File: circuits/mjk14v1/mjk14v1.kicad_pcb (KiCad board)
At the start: 2 copper layers, 56.6 x 57.7 mm, 34 parts, among them J1 9VDC, J2 GND, J3 Touch, J4 Touch GND, Q1 MMBT100, Q2 MMBT100, Q3 MMBT100, Q4 MMBT100, U1 4093, U2 4029, U3 BAW56LT1G, U4 BAW56LT1G

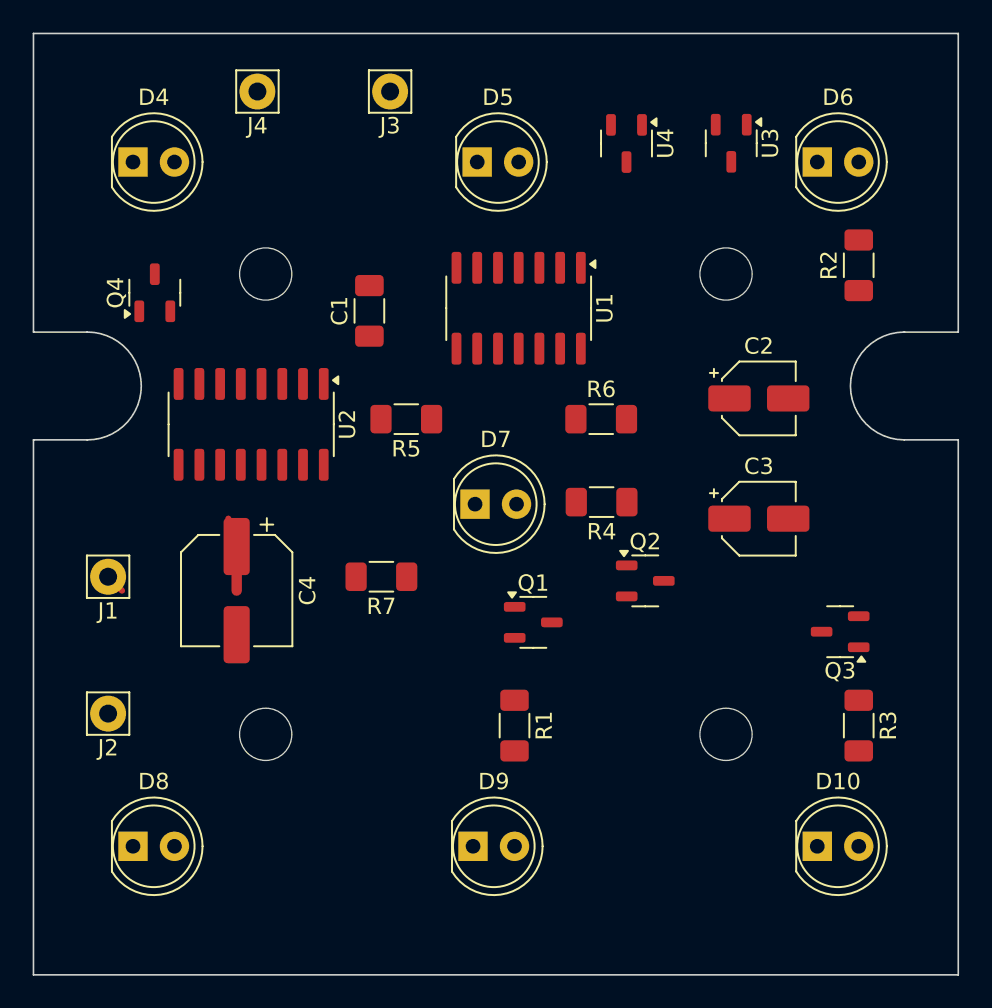
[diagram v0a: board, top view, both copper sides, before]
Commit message: Adding test points to the modernized JK14 design
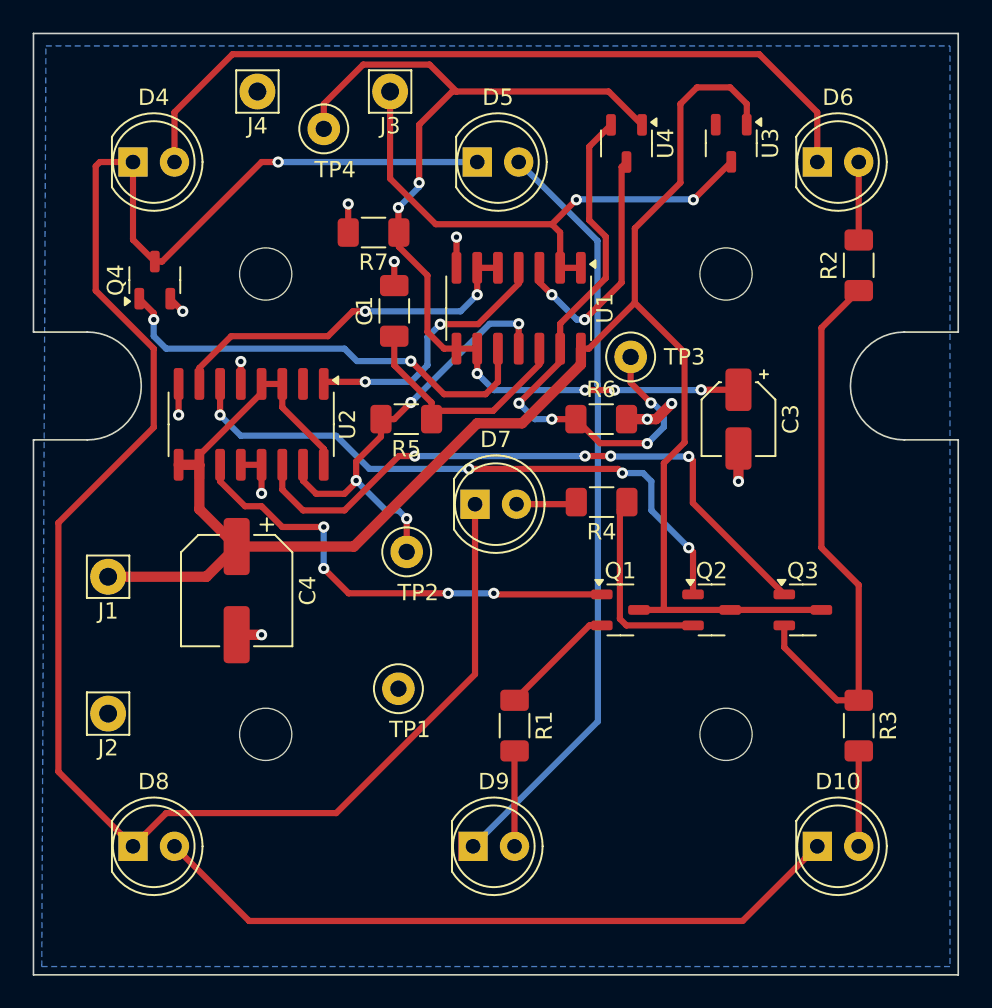
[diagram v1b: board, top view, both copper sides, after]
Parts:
- removed C2: 6.8uF/25V, Capacitor_SMD:CP_Elec_4x5.8
- added TP1: GND, TestPoint:TestPoint_Loop_D2.50mm_Drill1.0mm, F.Cu at (122.4, 82.5)
- added TP2: CK, TestPoint:TestPoint_Loop_D2.50mm_Drill1.0mm, F.Cu at (122.9, 74.1)
- added TP3: T1, TestPoint:TestPoint_Loop_D2.50mm_Drill1.0mm, F.Cu at (136.6, 62.2)
- added TP4: T2, TestPoint:TestPoint_Loop_D2.50mm_Drill1.0mm, F.Cu at (117.8, 48.2)
- moved R7 21.1 mm to (120.8, 54.5)
- moved C3 6.22 mm to (143.2, 66.0), turned to -90 degrees
- moved Q1 5.39 mm to (135.9, 77.6)
- moved Q2 4.44 mm to (141.5, 77.6)
- moved Q3 2.65 mm to (147.1, 77.6), turned to 0 degrees
- moved C1 1.52 mm to (122.1, 59.3)
- moved Q4 0.77 mm to (107.4, 57.4)
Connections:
- U1 pad 14: LVDC -> +9V
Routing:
- net Net-(D4-K): track 0.00 -> 114.5 mm, vias 0 -> 1
- net +9V: track 3.28 -> 112.1 mm
- net Net-(C3-Pad1): track 0.00 -> 62.1 mm, vias 0 -> 6
- net Net-(D4-A): track 0.00 -> 48.4 mm
- net Net-(D5-A): track 0.00 -> 47.1 mm
- net Net-(D10-K): track 0.00 -> 43.2 mm
- net Net-(Q3-B): track 0.00 -> 39.2 mm, vias 0 -> 4
- net Net-(Q2-B): track 0.00 -> 38.0 mm, vias 0 -> 4
- net Net-(R6-Pad1): track 0.00 -> 35.8 mm, vias 0 -> 4
- net Net-(Q3-E): track 0.00 -> 34.2 mm
- net Net-(J3-Pin_1): track 0.00 -> 33.1 mm, vias 0 -> 2
- net Net-(Q1-B): track 0.00 -> 28.8 mm, vias 0 -> 4
- net Net-(U2-CK): track 0.00 -> 27.8 mm, vias 0 -> 4
- net Net-(Q4-B): track 0.00 -> 27.6 mm, vias 0 -> 2
- net Net-(U2-Cout): track 0.00 -> 22.8 mm, vias 0 -> 2
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- added copper zone on B.Cu, net GND

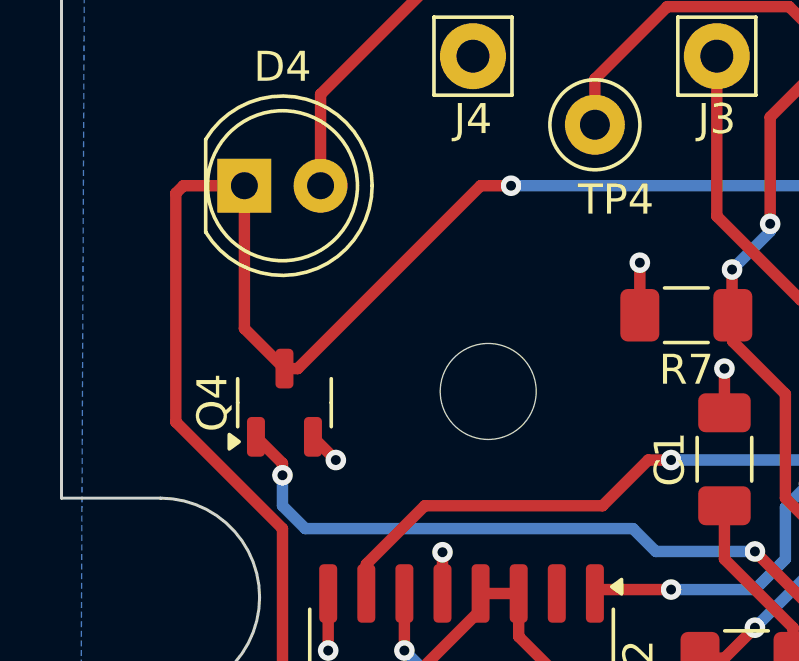
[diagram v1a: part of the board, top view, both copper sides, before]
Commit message: Fix wrong transistor in the modern JK14 circuit
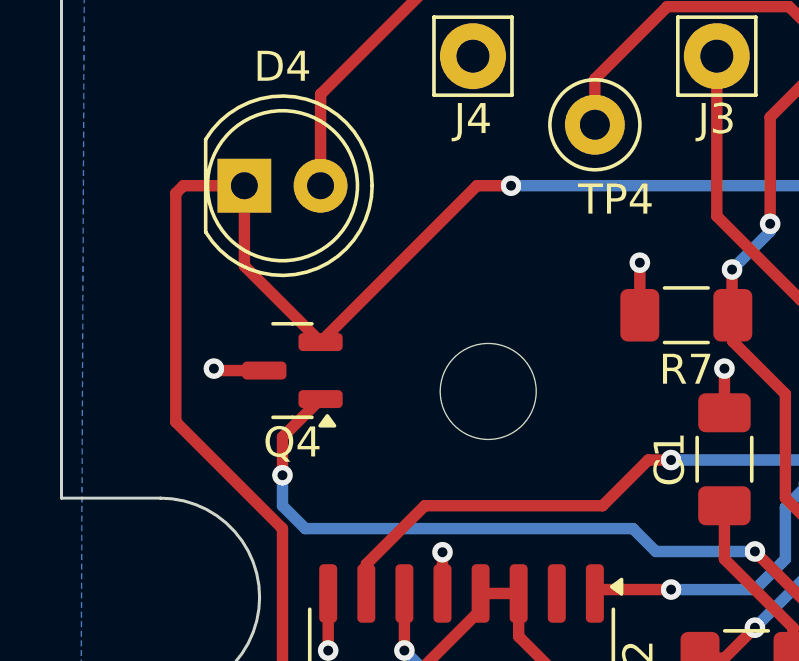
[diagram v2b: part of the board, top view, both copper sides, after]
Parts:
- Q4: value MMBT100 -> BC857; footprint Package_TO_SOT_SMD:SOT-23-3 -> Package_TO_SOT_SMD:SOT-23
- moved Q4 1.10 mm to (107.7, 56.4), turned to 180 degrees
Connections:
- Q4 pad 2: GND -> Net-(D4-K)
- Q4 pad 3: Net-(D4-K) -> GND
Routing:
- net Net-(D4-K): track 114.5 -> 112.5 mm
- net Net-(Q4-B): track 27.6 -> 29.0 mm
- net GND: track 19.2 -> 19.8 mm
